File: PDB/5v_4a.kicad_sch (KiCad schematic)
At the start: 15 parts, among them U16 INA228, U4 LM76005RNPR

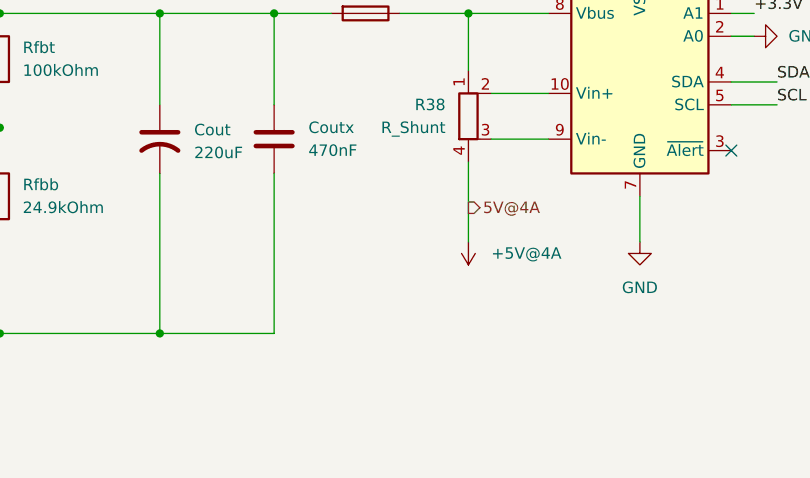
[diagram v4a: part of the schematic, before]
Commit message: added tp's, switches, inputs/outputs
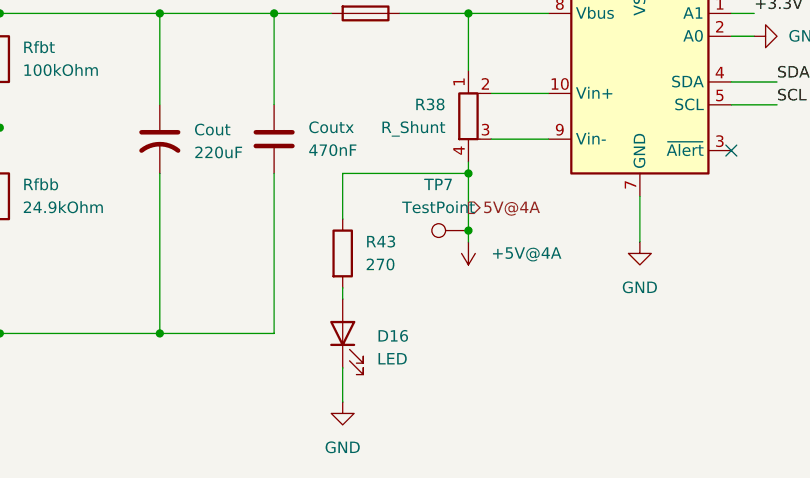
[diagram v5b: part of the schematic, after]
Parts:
- added D16: LED, LED_SMD:LED_0805_2012Metric, symbol Device:LED
- added R43: 270, Resistor_SMD:R_1206_3216Metric_Pad1.30x1.75mm_HandSolder, symbol Device:R
- added TP7: TestPoint, TestPoint:TestPoint_Pad_D2.0mm, symbol Connector:TestPoint
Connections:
- net +5V@4A: now also R43.1, TP7.1
- net AGND: now also D16.1 (K)
- new net: D16.2 (A), R43.2

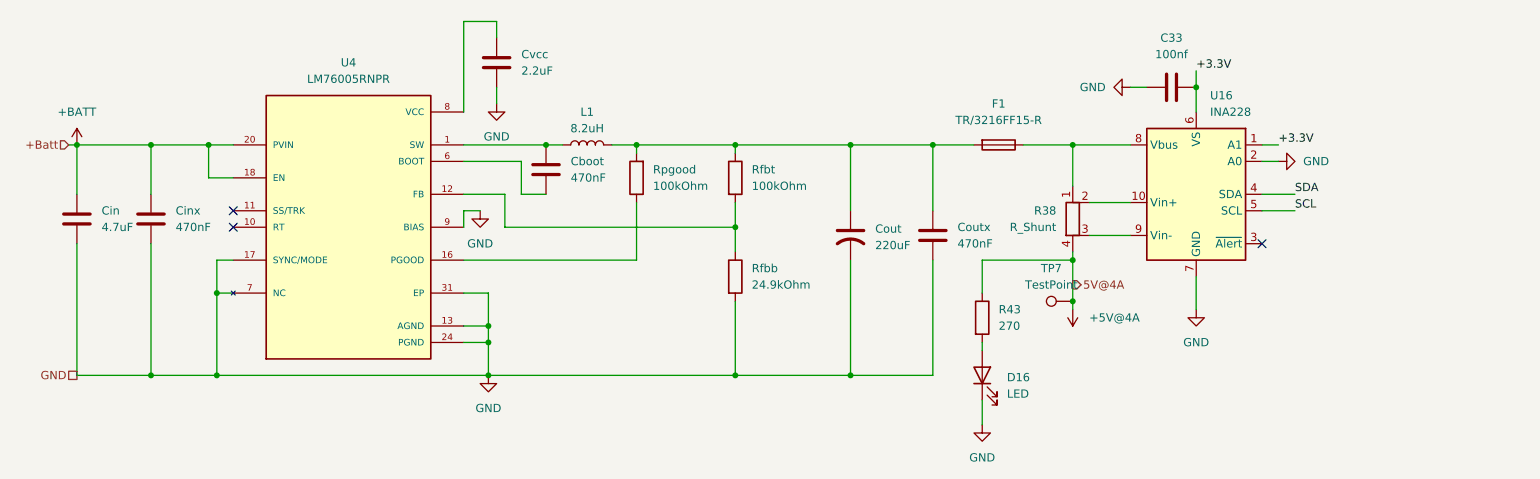
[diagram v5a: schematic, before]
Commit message: Finished all the footprints. doing poe myself now
finally.
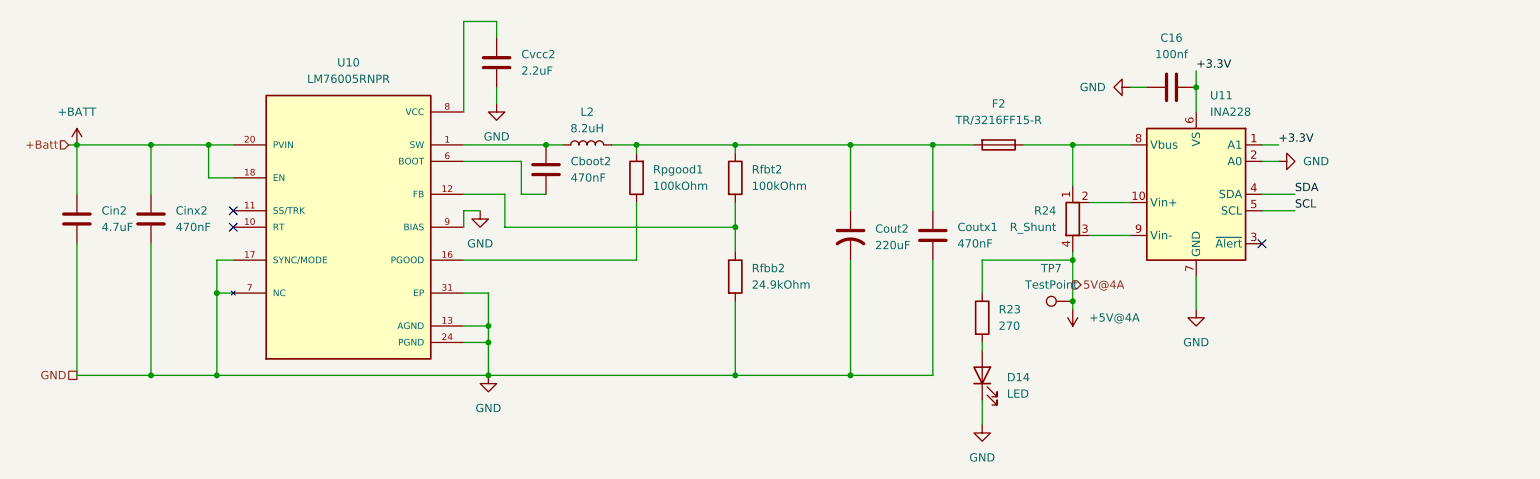
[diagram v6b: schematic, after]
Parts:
- C16: renamed from C33; footprint Capacitor_SMD:C_1206_3216Metric -> Capacitor_SMD:C_0603_1608Metric
- Cboot2: renamed from Cboot; footprint (none) -> Capacitor_SMD:C_0603_1608Metric
- Cin2: renamed from Cin; footprint (none) -> Capacitor_SMD:C_0603_1608Metric
- Cinx2: renamed from Cinx; footprint (none) -> Capacitor_SMD:C_0603_1608Metric
- Cout2: renamed from Cout; footprint (none) -> Capacitor_SMD:C_0603_1608Metric
- Coutx1: renamed from Coutx; footprint (none) -> Capacitor_SMD:C_0603_1608Metric
- Cvcc2: renamed from Cvcc; footprint (none) -> Capacitor_SMD:C_0603_1608Metric
- F2: renamed from F1; footprint (none) -> Fuse:Fuse_1206_3216Metric
- L2: renamed from L1; footprint (none) -> Inductor_SMD:L_1206_3216Metric
- R23: renamed from R43; footprint Resistor_SMD:R_1206_3216Metric_Pad1.30x1.75mm_HandSolder -> Resistor_SMD:R_0603_1608Metric
- R24: renamed from R38; footprint (none) -> Resistor_SMD:R_0603_1608Metric
- Rfbb2: renamed from Rfbb; footprint (none) -> Resistor_SMD:R_0603_1608Metric
- Rfbt2: renamed from Rfbt; footprint (none) -> Resistor_SMD:R_0603_1608Metric
- Rpgood1: renamed from Rpgood; footprint (none) -> Resistor_SMD:R_0603_1608Metric
- renumbered D16 to D14, U4 to U10, U16 to U11
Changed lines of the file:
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@@
 		(dnp no)
 		(fields_autoplaced yes)
-		(property "Reference" "R38"
+		(property "Reference" "R24"
 			(at 187.96 88.8999 0)
 			(show_name no)
@@
 			)
 		)
-		(property "Footprint" ""
+		(property "Footprint" "Resistor_SMD:R_0603_1608Metric"
 			(at 188.722 90.17 90)
 			(hide yes)
@@
 			(project "PDB"
 				(path "/a9cf05c4-aac5-4cf1-b700-1d3045f8dfbd/fb4943bd-b408-4249-996b-df676f2bb727"
-					(reference "R38")
+					(reference "R24")
 					(unit 1)
 				)
@@
 		(dnp no)
 		(fields_autoplaced yes)
-		(property "Reference" "Cinx"
+		(property "Reference" "Cinx2"
 			(at 52.07 88.8999 0)
 			(show_name no)
@@
 			)
 		)
-		(property "Footprint" ""
+		(property "Footprint" "Capacitor_SMD:C_0603_1608Metric"
 			(at 49.2252 93.98 0)
 			(hide yes)
@@
 			(project "PDB"
 				(path "/a9cf05c4-aac5-4cf1-b700-1d3045f8dfbd/fb4943bd-b408-4249-996b-df676f2bb727"
-					(reference "Cinx")
+					(reference "Cinx2")
 					(unit 1)
 				)
@@
 		(dnp no)
 		(fields_autoplaced yes)
-		(property "Reference" "Rfbt"
+		(property "Reference" "Rfbt2"
 			(at 140.97 82.5499 0)
 			(show_name no)
@@
 			)
 		)
-		(property "Footprint" ""
+		(property "Footprint" "Resistor_SMD:R_0603_1608Metric"
 			(at 136.652 83.82 90)
 			(hide yes)
@@
 			(project "PDB"
 				(path "/a9cf05c4-aac5-4cf1-b700-1d3045f8dfbd/fb4943bd-b408-4249-996b-df676f2bb727"
-					(reference "Rfbt")
+					(reference "Rfbt2")
 					(unit 1)
 				)
@@
 		(dnp no)
 		(fields_autoplaced yes)
-		(property "Reference" "U16"
+		(property "Reference" "U11"
 			(at 211.6933 71.12 0)
 			(show_name no)
@@
 			(project "PDB"
 				(path "/a9cf05c4-aac5-4cf1-b700-1d3045f8dfbd/fb4943bd-b408-4249-996b-df676f2bb727"
-					(reference "U16")
+					(reference "U11")
 					(unit 1)
 				)
@@
 		(dnp no)
 		(fields_autoplaced yes)
-		(property "Reference" "Coutx"
+		(property "Reference" "Coutx1"
 			(at 172.72 91.4399 0)
 			(show_name no)
@@
 			)
 		)
-		(property "Footprint" ""
+		(property "Footprint" "Capacitor_SMD:C_0603_1608Metric"
 			(at 169.8752 96.52 0)
 			(hide yes)
@@
 			(project "PDB"
 				(path "/a9cf05c4-aac5-4cf1-b700-1d3045f8dfbd/fb4943bd-b408-4249-996b-df676f2bb727"
-					(reference "Coutx")
+					(reference "Coutx1")
 					(unit 1)
 				)
@@
 		(dnp no)
 		(fields_autoplaced yes)
-		(property "Reference" "D16"
+		(property "Reference" "D14"
 			(at 180.34 114.6174 90)
 			(show_name no)
@@
 			(project "PDB"
 				(path "/a9cf05c4-aac5-4cf1-b700-1d3045f8dfbd/fb4943bd-b408-4249-996b-df676f2bb727"
-					(reference "D16")
+					(reference "D14")
 					(unit 1)
 				)
@@
 		(dnp no)
 		(fields_autoplaced yes)
-		(property "Reference" "Rpgood"
+		(property "Reference" "Rpgood1"
 			(at 125.73 82.5499 0)
 			(show_name no)
@@
 			)
 		)
-		(property "Footprint" ""
+		(property "Footprint" "Resistor_SMD:R_0603_1608Metric"
 			(at 124.968 83.82 90)
 			(hide yes)
@@
 			(project "PDB"
 				(path "/a9cf05c4-aac5-4cf1-b700-1d3045f8dfbd/fb4943bd-b408-4249-996b-df676f2bb727"
-					(reference "Rpgood")
+					(reference "Rpgood1")
 					(unit 1)
 				)
@@
 		(dnp no)
 		(fields_autoplaced yes)
-		(property "Reference" "L1"
+		(property "Reference" "L2"
 			(at 115.57 73.66 90)
 			(show_name no)
@@
 			)
 		)
-		(property "Footprint" ""
+		(property "Footprint" "Inductor_SMD:L_1206_3216Metric"
 			(at 115.57 78.74 0)
 			(hide yes)
@@
 			(project "PDB"
 				(path "/a9cf05c4-aac5-4cf1-b700-1d3045f8dfbd/fb4943bd-b408-4249-996b-df676f2bb727"
-					(reference "L1")
+					(reference "L2")
 					(unit 1)
 				)
@@
 		(dnp no)
 		(fields_autoplaced yes)
-		(property "Reference" "Rfbb"
+		(property "Reference" "Rfbb2"
 			(at 140.97 97.7899 0)
 			(show_name no)
@@
 			)
 		)
-		(property "Footprint" ""
+		(property "Footprint" "Resistor_SMD:R_0603_1608Metric"
 			(at 136.652 99.06 90)
 			(hide yes)
@@
 			(project "PDB"
 				(path "/a9cf05c4-aac5-4cf1-b700-1d3045f8dfbd/fb4943bd-b408-4249-996b-df676f2bb727"
-					(reference "Rfbb")
+					(reference "Rfbb2")
 					(unit 1)
 				)
@@
 		(dnp no)
 		(fields_autoplaced yes)
-		(property "Reference" "C33"
+		(property "Reference" "C16"
 			(at 205.74 62.23 90)
 			(show_name no)
@@
 			)
 		)
-		(property "Footprint" "Capacitor_SMD:C_1206_3216Metric"
+		(property "Footprint" "Capacitor_SMD:C_0603_1608Metric"
 			(at 209.55 68.8848 0)
 			(hide yes)
@@
 			(project "PDB"
 				(path "/a9cf05c4-aac5-4cf1-b700-1d3045f8dfbd/fb4943bd-b408-4249-996b-df676f2bb727"
-					(reference "C33")
+					(reference "C16")
 					(unit 1)
 				)
@@
 		(dnp no)
 		(fields_autoplaced yes)
-		(property "Reference" "Cvcc"
+		(property "Reference" "Cvcc2"
 			(at 105.41 64.7699 0)
 			(show_name no)
@@
 			)
 		)
-		(property "Footprint" ""
+		(property "Footprint" "Capacitor_SMD:C_0603_1608Metric"
 			(at 102.5652 69.85 0)
 			(hide yes)
@@
 			(project "PDB"
 				(path "/a9cf05c4-aac5-4cf1-b700-1d3045f8dfbd/fb4943bd-b408-4249-996b-df676f2bb727"
-					(reference "Cvcc")
+					(reference "Cvcc2")
 					(unit 1)
 				)
@@
 		(dnp no)
 		(fields_autoplaced yes)
-		(property "Reference" "F1"
+		(property "Reference" "F2"
 			(at 179.07 72.39 90)
 			(show_name no)
@@
 			)
 		)
-		(property "Footprint" ""
+		(property "Footprint" "Fuse:Fuse_1206_3216Metric"
 			(at 179.07 76.962 90)
 			(hide yes)
@@
 			(project "PDB"
 				(path "/a9cf05c4-aac5-4cf1-b700-1d3045f8dfbd/fb4943bd-b408-4249-996b-df676f2bb727"
-					(reference "F1")
+					(reference "F2")
 					(unit 1)
 				)
@@
 		(dnp no)
 		(fields_autoplaced yes)
-		(property "Reference" "Cout"
+		(property "Reference" "Cout2"
 			(at 160.02 91.6939 0)
 			(show_name no)
@@
 			)
 		)
-		(property "Footprint" ""
+		(property "Footprint" "Capacitor_SMD:C_0603_1608Metric"
 			(at 156.21 92.71 0)
 			(hide yes)
@@
 			(project "PDB"
 				(path "/a9cf05c4-aac5-4cf1-b700-1d3045f8dfbd/fb4943bd-b408-4249-996b-df676f2bb727"
-					(reference "Cout")
+					(reference "Cout2")
 					(unit 1)
 				)
@@
 		(dnp no)
 		(fields_autoplaced yes)
-		(property "Reference" "Cboot"
+		(property "Reference" "Cboot2"
 			(at 113.03 81.2799 0)
 			(show_name no)
@@
 			)
 		)
-		(property "Footprint" ""
+		(property "Footprint" "Capacitor_SMD:C_0603_1608Metric"
 			(at 110.1852 86.36 0)
 			(hide yes)
@@
 			(project "PDB"
 				(path "/a9cf05c4-aac5-4cf1-b700-1d3045f8dfbd/fb4943bd-b408-4249-996b-df676f2bb727"
-					(reference "Cboot")
+					(reference "Cboot2")
 					(unit 1)
 				)
@@
 		(dnp no)
 		(fields_autoplaced yes)
-		(property "Reference" "U4"
+		(property "Reference" "U10"
 			(at 78.74 66.04 0)
 			(show_name no)
@@
 			(project "PDB"
 				(path "/a9cf05c4-aac5-4cf1-b700-1d3045f8dfbd/fb4943bd-b408-4249-996b-df676f2bb727"
-					(reference "U4")
+					(reference "U10")
 					(unit 1)
 				)
@@
 		(dnp no)
 		(fields_autoplaced yes)
-		(property "Reference" "Cin"
+		(property "Reference" "Cin2"
 			(at 40.64 88.8999 0)
 			(show_name no)
@@
 			)
 		)
-		(property "Footprint" ""
+		(property "Footprint" "Capacitor_SMD:C_0603_1608Metric"
 			(at 37.7952 93.98 0)
 			(hide yes)
@@
 			(project "PDB"
 				(path "/a9cf05c4-aac5-4cf1-b700-1d3045f8dfbd/fb4943bd-b408-4249-996b-df676f2bb727"
-					(reference "Cin")
+					(reference "Cin2")
 					(unit 1)
 				)
@@
 		(in_pos_files yes)
 		(dnp no)
-		(property "Reference" "R43"
+		(property "Reference" "R23"
 			(at 179.07 104.1399 0)
 			(show_name no)
@@
 			)
 		)
-		(property "Footprint" "Resistor_SMD:R_1206_3216Metric_Pad1.30x1.75mm_HandSolder"
+		(property "Footprint" "Resistor_SMD:R_0603_1608Metric"
 			(at 174.752 105.41 90)
 			(hide yes)
@@
 			(project "PDB"
 				(path "/a9cf05c4-aac5-4cf1-b700-1d3045f8dfbd/fb4943bd-b408-4249-996b-df676f2bb727"
-					(reference "R43")
-					(unit 1)
-				)
+					(reference "R23")
+					(unit 1)
+				)

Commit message: more footprint
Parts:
- U10: footprint foot:LM76005RNPR -> Dependencies:LM76005RNPR
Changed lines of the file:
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@@
 			)
 		)
-		(property "Footprint" "foot:LM76005RNPR"
+		(property "Footprint" "Dependencies:LM76005RNPR"
 			(at 78.74 91.44 0)
 			(hide yes)

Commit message: fixed component footprints
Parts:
- R24: footprint Resistor_SMD:R_0603_1608Metric -> Resistor_SMD:R_Shunt_Vishay_WSR2_WSR3_KelvinConnection
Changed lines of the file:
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@@
 			)
 		)
-		(property "Footprint" "Resistor_SMD:R_0603_1608Metric"
+		(property "Footprint" "Resistor_SMD:R_Shunt_Vishay_WSR2_WSR3_KelvinConnection"
 			(at 188.722 90.17 90)
 			(hide yes)
@@
 		(dnp no)
 		(fields_autoplaced yes)
-		(property "Reference" "#PWR055"
+		(property "Reference" "#PWR054"
 			(at 193.04 69.85 0)
 			(hide yes)
@@
 			(project "PDB"
 				(path "/a9cf05c4-aac5-4cf1-b700-1d3045f8dfbd/fb4943bd-b408-4249-996b-df676f2bb727"
-					(reference "#PWR055")
+					(reference "#PWR054")
 					(unit 1)
 				)
@@
 		(dnp no)
 		(fields_autoplaced yes)
-		(property "Reference" "#PWR01"
+		(property "Reference" "#PWR050"
 			(at 100.33 120.65 0)
 			(hide yes)
@@
 			(project "PDB"
 				(path "/a9cf05c4-aac5-4cf1-b700-1d3045f8dfbd/fb4943bd-b408-4249-996b-df676f2bb727"
-					(reference "#PWR01")
+					(reference "#PWR050")
 					(unit 1)
 				)
@@
 		(dnp no)
 		(fields_autoplaced yes)
-		(property "Reference" "#PWR062"
+		(property "Reference" "#PWR056"
 			(at 228.6 81.28 0)
 			(hide yes)
@@
 			(project "PDB"
 				(path "/a9cf05c4-aac5-4cf1-b700-1d3045f8dfbd/fb4943bd-b408-4249-996b-df676f2bb727"
-					(reference "#PWR062")
+					(reference "#PWR056")
 					(unit 1)
 				)
@@
 		(dnp no)
 		(fields_autoplaced yes)
-		(property "Reference" "#PWR03"
+		(property "Reference" "#PWR051"
 			(at 101.6 78.74 0)
 			(hide yes)
@@
 			(project "PDB"
 				(path "/a9cf05c4-aac5-4cf1-b700-1d3045f8dfbd/fb4943bd-b408-4249-996b-df676f2bb727"
-					(reference "#PWR03")
+					(reference "#PWR051")
 					(unit 1)
 				)
@@
 		(dnp no)
 		(fields_autoplaced yes)
-		(property "Reference" "#PWR02"
+		(property "Reference" "#PWR049"
 			(at 99.06 95.25 0)
 			(hide yes)
@@
 			(project "PDB"
 				(path "/a9cf05c4-aac5-4cf1-b700-1d3045f8dfbd/fb4943bd-b408-4249-996b-df676f2bb727"
-					(reference "#PWR02")
+					(reference "#PWR049")
 					(unit 1)
 				)
@@
 		(dnp no)
 		(fields_autoplaced yes)
-		(property "Reference" "#PWR070"
+		(property "Reference" "#PWR052"
 			(at 176.53 128.27 0)
 			(hide yes)
@@
 			(project "PDB"
 				(path "/a9cf05c4-aac5-4cf1-b700-1d3045f8dfbd/fb4943bd-b408-4249-996b-df676f2bb727"
-					(reference "#PWR070")
+					(reference "#PWR052")
 					(unit 1)
 				)
@@
 		(dnp no)
 		(fields_autoplaced yes)
-		(property "Reference" "#PWR057"
+		(property "Reference" "#PWR055"
 			(at 209.55 110.49 0)
 			(hide yes)
@@
 			(project "PDB"
 				(path "/a9cf05c4-aac5-4cf1-b700-1d3045f8dfbd/fb4943bd-b408-4249-996b-df676f2bb727"
-					(reference "#PWR057")
+					(reference "#PWR055")
 					(unit 1)
 				)
@@
 		(dnp no)
 		(fields_autoplaced yes)
-		(property "Reference" "#PWR011"
+		(property "Reference" "#PWR048"
 			(at 36.83 82.55 0)
 			(hide yes)
@@
 			(project "PDB"
 				(path "/a9cf05c4-aac5-4cf1-b700-1d3045f8dfbd/fb4943bd-b408-4249-996b-df676f2bb727"
-					(reference "#PWR011")
+					(reference "#PWR048")
 					(unit 1)
 				)
@@
 		(dnp no)
 		(fields_autoplaced yes)
-		(property "Reference" "#PWR010"
+		(property "Reference" "#PWR053"
 			(at 190.5 100.33 0)
 			(hide yes)
@@
 			(project "PDB"
 				(path "/a9cf05c4-aac5-4cf1-b700-1d3045f8dfbd/fb4943bd-b408-4249-996b-df676f2bb727"
-					(reference "#PWR010")
-					(unit 1)
-				)
+					(reference "#PWR053")
+					(unit 1)
+				)
